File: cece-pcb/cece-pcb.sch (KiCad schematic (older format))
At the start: 26 parts, among them J1 SERIAL, J2 HTU21D, J3 Li-Ion Battery, J4 VAC, K1 SANYOU_SRD_Form_C, Q2 Q_NPN, U2 MCP73811T-420I-OT, U3 TLV75533PDBV

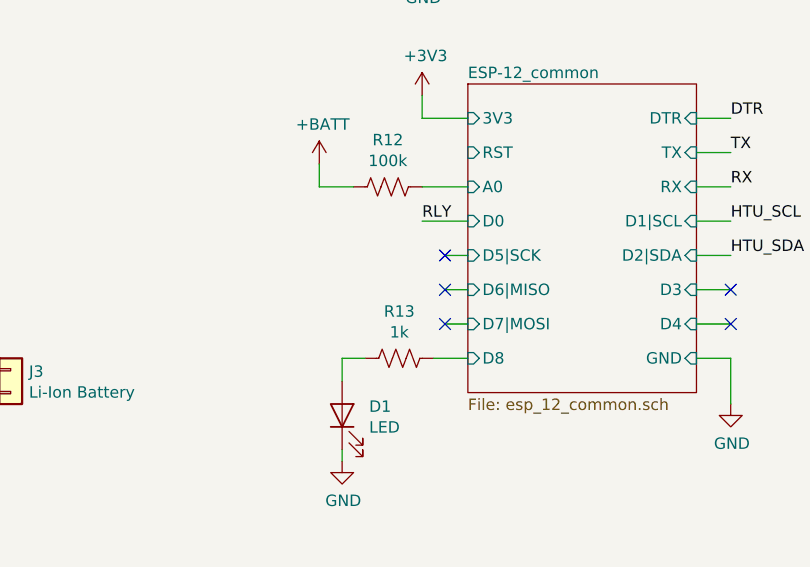
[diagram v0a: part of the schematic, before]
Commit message: Complete ESP-12 part of the PCB
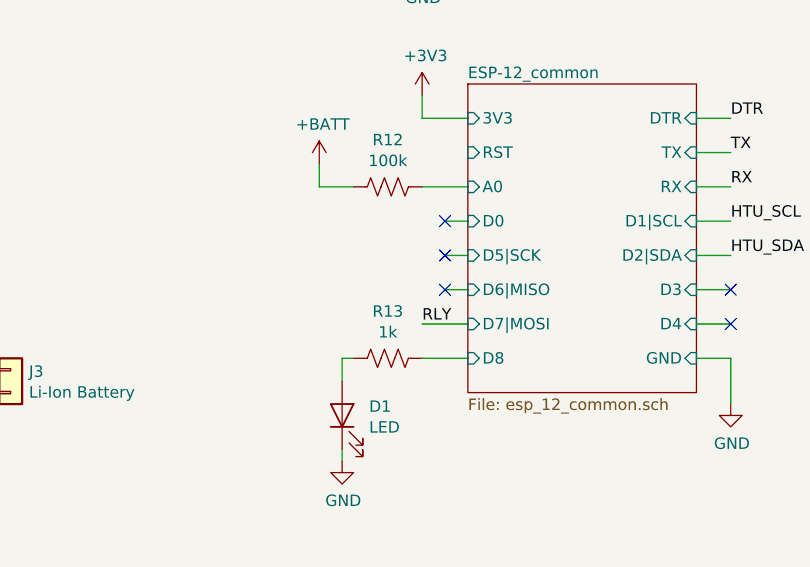
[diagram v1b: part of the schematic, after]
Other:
- moved on the sheet: R13
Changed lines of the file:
@@
 $EndSheet
 Wire Wire Line
-	5300 4150 5100 4150
+	5300 4600 5100 4600
 Wire Wire Line
 	6300 4150 6450 4150
 Wire Wire Line
 	6300 4300 6450 4300
-Text Label 5100 4150 0    50   ~ 0
+Text Label 5100 4600 0    50   ~ 0
 RLY
 Text Label 6450 4150 0    50   ~ 0
@@
 L Device:R_US R13
 U 1 1 5FE041BA
-P 5000 4750
-F 0 "R13" V 4795 4750 50  0000 C CNN
-F 1 "1k" V 4886 4750 50  0000 C CNN
-F 2 "Resistor_THT:R_Axial_DIN0207_L6.3mm_D2.5mm_P7.62mm_Horizontal" V 5040 4740 50  0001 C CNN
-F 3 "~" H 5000 4750 50  0001 C CNN
-	1    5000 4750
+P 4950 4750
+F 0 "R13" V 4745 4750 50  0000 C CNN
+F 1 "1k" V 4836 4750 50  0000 C CNN
+F 2 "Resistor_THT:R_Axial_DIN0207_L6.3mm_D2.5mm_P7.62mm_Horizontal" V 4990 4740 50  0001 C CNN
+F 3 "~" H 4950 4750 50  0001 C CNN
+	1    4950 4750
 	0    1    1    0
 $EndComp
@@
 $EndComp
 Wire Wire Line
-	5300 4750 5150 4750
-Wire Wire Line
-	4850 4750 4750 4750
+	5300 4750 5100 4750
+Wire Wire Line
+	4800 4750 4750 4750
 Wire Wire Line
 	4750 4750 4750 4850
@@
 NoConn ~ 5200 4300
 NoConn ~ 5200 4450
-NoConn ~ 5200 4600
+NoConn ~ 5200 4150
 NoConn ~ 6450 4600
 NoConn ~ 6450 4450
@@
 	5200 4450 5300 4450
 Wire Wire Line
-	5200 4600 5300 4600
+	5200 4150 5300 4150
 Wire Wire Line
 	6450 4600 6300 4600

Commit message: Finish first board revision
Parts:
- removed JP12: RLY_VCC, Jumper:SolderJumper-3_P1.3mm_Bridged12_Pad1.0x1.5mm, symbol Jumper:SolderJumper_3_Bridged12
- removed R12: 100k, Resistor_THT:R_Axial_DIN0207_L6.3mm_D2.5mm_P7.62mm_Horizontal, symbol Device:R_US
- added JP2: VBATT_A0, Jumper:SolderJumper-2_P1.3mm_Bridged_Pad1.0x1.5mm, symbol Jumper:SolderJumper_2_Bridged
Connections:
- wire segments 100 -> 90
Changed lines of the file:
@@
-	1    0    0    -1
-$EndComp
-$Comp
-L power:+3V3 #PWR018
-U 1 1 5FD89DF7
-P 7800 3050
-F 0 "#PWR018" H 7800 2900 50  0001 C CNN
-F 1 "+3V3" H 7815 3223 50  0000 C CNN
-F 2 "" H 7800 3050 50  0001 C CNN
-F 3 "" H 7800 3050 50  0001 C CNN
-	1    7800 3050
-	1    0    0    -1
-$EndComp
-$Comp
-L power:+5V #PWR019
-U 1 1 5FD8A15A
-P 8250 3050
-F 0 "#PWR019" H 8250 2900 50  0001 C CNN
-F 1 "+5V" H 8265 3223 50  0000 C CNN
-F 2 "" H 8250 3050 50  0001 C CNN
-F 3 "" H 8250 3050 50  0001 C CNN
-	1    8250 3050
 	1    0    0    -1
 $EndComp
@@
 	10200 2800 10050 2800
 Wire Wire Line
-	10050 2800 10050 2500
-Wire Wire Line
-	10050 2500 9150 2500
-Wire Wire Line
-	9150 2500 9150 2800
-Wire Wire Line
 	9150 2800 9300 2800
-Wire Wire Line
-	9000 3000 9000 2400
-Wire Wire Line
-	9000 2400 10150 2400
-Wire Wire Line
-	10150 2400 10150 2700
-Wire Wire Line
-	10150 2700 10200 2700
 $Comp
 L Converter_ACDC:HLK-PM01 PS1
@@
 Text Label 10050 3000 0    50   ~ 0
 LN
+Text Label 10050 2700 0    50   ~ 0
+NO
 Text Label 10050 2800 0    50   ~ 0
-NO
-Text Label 10050 2400 0    50   ~ 0
 NC
 Wire Wire Line
@@
 	8550 3800 8550 3750
 Wire Wire Line
-	9000 3000 9300 3000
+	9150 3000 9300 3000
 $Comp
 L Battery_Management:MCP73811T-420I-OT U2
@@
 Wire Wire Line
 	2550 5100 2550 5200
-$Comp
-L Device:R_US R12
-U 1 1 5FDFCF50
-P 4950 4000
-F 0 "R12" V 4745 4000 50  0000 C CNN
-F 1 "100k" V 4836 4000 50  0000 C CNN
-F 2 "Resistor_THT:R_Axial_DIN0207_L6.3mm_D2.5mm_P7.62mm_Horizontal" V 4990 3990 50  0001 C CNN
-F 3 "~" H 4950 4000 50  0001 C CNN
-	1    4950 4000
-	0    1    1    0
-$EndComp
 Wire Wire Line
 	5100 4000 5300 4000
-$Comp
-L power:+BATT #PWR023
-U 1 1 5FDFFC00
-P 4650 3900
-F 0 "#PWR023" H 4650 3750 50  0001 C CNN
-F 1 "+BATT" H 4665 4073 50  0000 C CNN
-F 2 "" H 4650 3900 50  0001 C CNN
-F 3 "" H 4650 3900 50  0001 C CNN
-	1    4650 3900
-	1    0    0    -1
-$EndComp
-Wire Wire Line
-	4650 3900 4650 4000
 Wire Wire Line
 	4650 4000 4800 4000
@@
 Wire Wire Line
 	8250 5650 8000 5650
-$Comp
-L Jumper:SolderJumper_3_Bridged12 JP12
-U 1 1 5FD8AB22
-P 8250 3300
-F 0 "JP12" V 8204 3368 50  0000 L CNN
-F 1 "RLY_VCC" V 8295 3368 50  0000 L CNN
-F 2 "Jumper:SolderJumper-3_P1.3mm_Bridged12_Pad1.0x1.5mm" H 8250 3300 50  0001 C CNN
-F 3 "~" H 8250 3300 50  0001 C CNN
-	1    8250 3300
-	0    -1   1    0
-$EndComp
-Wire Wire Line
-	8550 3300 8400 3300
-Connection ~ 8550 3300
-Wire Wire Line
-	8250 3050 8250 3100
-Wire Wire Line
-	7800 3050 7800 3500
-Wire Wire Line
-	7800 3500 8250 3500
+Wire Wire Line
+	10050 2700 10200 2700
+Text Label 9150 2800 0    50   ~ 0
+NO
+Text Label 9150 3000 0    50   ~ 0
+NC
+$Comp
+L Jumper:SolderJumper_2_Bridged JP2
+U 1 1 5FCD2589
+P 4950 4000
+F 0 "JP2" H 4950 4205 50  0000 C CNN
+F 1 "VBATT_A0" H 4950 4114 50  0000 C CNN
+F 2 "Jumper:SolderJumper-2_P1.3mm_Bridged_Pad1.0x1.5mm" H 4950 4000 50  0001 C CNN
+F 3 "~" H 4950 4000 50  0001 C CNN
+	1    4950 4000
+	1    0    0    -1
+$EndComp
+Wire Wire Line
+	4650 3900 4650 4000
+$Comp
+L power:+BATT #PWR023
+U 1 1 5FDFFC00
+P 4650 3900
+F 0 "#PWR023" H 4650 3750 50  0001 C CNN
+F 1 "+BATT" H 4665 4073 50  0000 C CNN
+F 2 "" H 4650 3900 50  0001 C CNN
+F 3 "" H 4650 3900 50  0001 C CNN
+	1    4650 3900
+	1    0    0    -1
+$EndComp
+$Comp
+L power:+BATT #PWR?
+U 1 1 5FD3EF92
+P 9200 3300
+F 0 "#PWR?" H 9200 3150 50  0001 C CNN
+F 1 "+BATT" H 9215 3473 50  0000 C CNN
+F 2 "" H 9200 3300 50  0001 C CNN
+F 3 "" H 9200 3300 50  0001 C CNN
+	1    9200 3300
+	1    0    0    -1
+$EndComp
 $EndSCHEMATC

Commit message: More touches to the layout. Almost finished
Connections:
- net +3V3: now also J1.1 (Pin_1); no longer J1.5 (Pin_5)
- net GND: now also J1.5 (Pin_5); no longer J1.1 (Pin_1)
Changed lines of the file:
@@
 $EndComp
-Wire Wire Line
-	5100 2600 5250 2600
 Wire Wire Line
 	5100 2700 5250 2700
@@
 Wire Wire Line
 	5250 2900 5100 2900
-Wire Wire Line
-	5100 3000 5250 3000
 $Comp
 L power:+3V3 #PWR0103
 U 1 1 5FD72E0B
-P 5100 2600
-F 0 "#PWR0103" H 5100 2450 50  0001 C CNN
-F 1 "+3V3" H 5115 2773 50  0000 C CNN
-F 2 "" H 5100 2600 50  0001 C CNN
-F 3 "" H 5100 2600 50  0001 C CNN
-	1    5100 2600
+P 4700 3000
+F 0 "#PWR0103" H 4700 2850 50  0001 C CNN
+F 1 "+3V3" H 4715 3173 50  0000 C CNN
+F 2 "" H 4700 3000 50  0001 C CNN
+F 3 "" H 4700 3000 50  0001 C CNN
+	1    4700 3000
 	1    0    0    -1
 $EndComp
@@
 L power:GND #PWR0104
 U 1 1 5FD73334
-P 5100 3000
-F 0 "#PWR0104" H 5100 2750 50  0001 C CNN
-F 1 "GND" H 5105 2827 50  0000 C CNN
-F 2 "" H 5100 3000 50  0001 C CNN
-F 3 "" H 5100 3000 50  0001 C CNN
-	1    5100 3000
+P 4950 2600
+F 0 "#PWR0104" H 4950 2350 50  0001 C CNN
+F 1 "GND" H 4955 2427 50  0000 C CNN
+F 2 "" H 4950 2600 50  0001 C CNN
+F 3 "" H 4950 2600 50  0001 C CNN
+	1    4950 2600
 	1    0    0    -1
 $EndComp
@@
 $EndComp
 $Comp
-L power:+BATT #PWR?
+L power:+BATT #PWR0109
 U 1 1 5FD3EF92
 P 9200 3300
-F 0 "#PWR?" H 9200 3150 50  0001 C CNN
+F 0 "#PWR0109" H 9200 3150 50  0001 C CNN
 F 1 "+BATT" H 9215 3473 50  0000 C CNN
 F 2 "" H 9200 3300 50  0001 C CNN
@@
 	1    0    0    -1
 $EndComp
+Wire Wire Line
+	4950 2600 5250 2600
+Wire Wire Line
+	4700 3000 5250 3000
 $EndSCHEMATC

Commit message: Add jumper to send 5V directly to the LDO if no battery is installed
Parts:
- added JP3: VBATT 5V, Jumper:SolderJumper-2_P1.3mm_Open_Pad1.0x1.5mm, symbol Jumper:SolderJumper_2_Open
- J4: footprint TerminalBlock:TerminalBlock_bornier-4_P5.08mm -> TerminalBlock:TerminalBlock_bornier-5_P5.08mm; symbol Connector:Screw_Terminal_01x04 -> Connector:Screw_Terminal_01x05
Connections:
- net +5V: now also JP3.1 (A)
- net +BATT: now also JP3.2 (B)
- net C: now also J4.2 (Pin_2); no longer J4.3 (Pin_3), PS1.2 (AC/N)
- net NC: now also J4.3 (Pin_3); no longer J4.2 (Pin_2)
- net LN renamed ACL
- net ACL: now also J4.5 (Pin_5); no longer J4.4 (Pin_4)
- new net ACN: J4.4 (Pin_4), PS1.2 (AC/N)
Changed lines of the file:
@@
 RLY
 $Comp
-L Connector:Screw_Terminal_01x04 J4
+L Connector:Screw_Terminal_01x05 J4
 U 1 1 5FD96487
-P 10400 2800
-F 0 "J4" H 10480 2792 50  0000 L CNN
-F 1 "VAC" H 10480 2701 50  0000 L CNN
-F 2 "TerminalBlock:TerminalBlock_bornier-4_P5.08mm" H 10400 2800 50  0001 C CNN
-F 3 "~" H 10400 2800 50  0001 C CNN
-	1    10400 2800
-	1    0    0    -1
-$EndComp
-Wire Wire Line
-	10200 2900 9900 2900
-Wire Wire Line
-	10200 2800 10050 2800
+P 10450 2250
+F 0 "J4" H 10530 2242 50  0000 L CNN
+F 1 "VAC" H 10530 2151 50  0000 L CNN
+F 2 "TerminalBlock:TerminalBlock_bornier-5_P5.08mm" H 10450 2250 50  0001 C CNN
+F 3 "~" H 10450 2250 50  0001 C CNN
+	1    10450 2250
+	1    0    0    -1
+$EndComp
+Wire Wire Line
+	10250 2250 10100 2250
 Wire Wire Line
 	9150 2800 9300 2800
@@
 $EndComp
 Wire Wire Line
-	10200 3000 10050 3000
-Text Label 10050 2900 0    50   ~ 0
+	10250 2450 10100 2450
+Text Label 10000 2900 0    50   ~ 0
 C
-Text Label 10050 3000 0    50   ~ 0
-LN
-Text Label 10050 2700 0    50   ~ 0
+Text Label 10100 2050 0    50   ~ 0
 NO
-Text Label 10050 2800 0    50   ~ 0
+Text Label 10100 2250 0    50   ~ 0
 NC
 Wire Wire Line
-	1400 2750 1300 2750
-Wire Wire Line
-	1400 2950 1300 2950
-Text Label 1300 2750 0    50   ~ 0
-LN
-Text Label 1300 2950 0    50   ~ 0
-C
+	1400 2750 1250 2750
 $Comp
 L power:GND #PWR015
@@
 P 2000 4700
 F 0 "U2" H 2150 4600 50  0000 L CNN
-F 1 "MCP73811T-420I-OT" H 2050 4950 50  0000 L CNN
+F 1 "MCP73811T-420I-OT" H 1700 4400 50  0000 L CNN
 F 2 "Package_TO_SOT_SMD:SOT-23-5" H 2050 4450 50  0001 L CNN
 F 3 "http://ww1.microchip.com/downloads/en/DeviceDoc/22036b.pdf" H 1750 4950 50  0001 C CNN
@@
 	8250 5650 8000 5650
 Wire Wire Line
-	10050 2700 10200 2700
+	10100 2150 10250 2150
 Text Label 9150 2800 0    50   ~ 0
 NO
@@
 Wire Wire Line
 	4700 3000 5250 3000
+Wire Wire Line
+	9900 2900 10000 2900
+Wire Wire Line
+	10100 2350 10250 2350
+Wire Wire Line
+	10100 2050 10250 2050
+Text Label 10100 2150 0    50   ~ 0
+C
+Text Label 1250 2750 0    50   ~ 0
+ACL
+Text Label 1250 2950 0    50   ~ 0
+ACN
+Wire Wire Line
+	1250 2950 1400 2950
+Text Label 10100 2450 0    50   ~ 0
+ACL
+Text Label 10100 2350 0    50   ~ 0
+ACN
+$Comp
+L Jumper:SolderJumper_2_Open JP3
+U 1 1 5FD1A80F
+P 2300 4350
+F 0 "JP3" H 2300 4555 50  0000 C CNN
+F 1 "VBATT 5V" H 2300 4464 50  0000 C CNN
+F 2 "Jumper:SolderJumper-2_P1.3mm_Open_Pad1.0x1.5mm" H 2300 4350 50  0001 C CNN
+F 3 "~" H 2300 4350 50  0001 C CNN
+	1    2300 4350
+	1    0    0    -1
+$EndComp
+Wire Wire Line
+	2150 4350 2000 4350
+Wire Wire Line
+	2550 4350 2550 4600
+Wire Wire Line
+	2550 4350 2450 4350
 $EndSCHEMATC

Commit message: Fix wrong footprint for the pin headers
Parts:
- J1: footprint Connector_PinHeader_1.27mm:PinHeader_1x05_P1.27mm_Vertical -> Connector_PinHeader_2.54mm:PinHeader_1x05_P2.54mm_Vertical
- J2: footprint Connector_PinHeader_1.27mm:PinHeader_1x04_P1.27mm_Vertical -> Connector_PinHeader_2.54mm:PinHeader_1x04_P2.54mm_Vertical
- J3: footprint Connector_PinHeader_1.27mm:PinHeader_1x02_P1.27mm_Vertical -> Connector_PinHeader_2.54mm:PinHeader_1x02_P2.54mm_Vertical
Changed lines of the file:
@@
 F 0 "J1" H 5422 2732 50  0000 R CNN
 F 1 "SERIAL" H 5422 2823 50  0000 R CNN
-F 2 "Connector_PinHeader_1.27mm:PinHeader_1x05_P1.27mm_Vertical" H 5450 2800 50  0001 C CNN
+F 2 "Connector_PinHeader_2.54mm:PinHeader_1x05_P2.54mm_Vertical" H 5450 2800 50  0001 C CNN
 F 3 "~" H 5450 2800 50  0001 C CNN
 	1    5450 2800
@@
 F 0 "J2" H 6628 2726 50  0000 L CNN
 F 1 "HTU21D" H 6628 2635 50  0000 L CNN
-F 2 "Connector_PinHeader_1.27mm:PinHeader_1x04_P1.27mm_Vertical" H 6600 2750 50  0001 C CNN
+F 2 "Connector_PinHeader_2.54mm:PinHeader_1x04_P2.54mm_Vertical" H 6600 2750 50  0001 C CNN
 F 3 "~" H 6600 2750 50  0001 C CNN
 	1    6600 2750
@@
 F 0 "J3" H 3380 4792 50  0000 L CNN
 F 1 "Li-Ion Battery" H 3380 4701 50  0000 L CNN
-F 2 "Connector_PinHeader_1.27mm:PinHeader_1x02_P1.27mm_Vertical" H 3300 4800 50  0001 C CNN
+F 2 "Connector_PinHeader_2.54mm:PinHeader_1x02_P2.54mm_Vertical" H 3300 4800 50  0001 C CNN
 F 3 "~" H 3300 4800 50  0001 C CNN
 	1    3300 4800

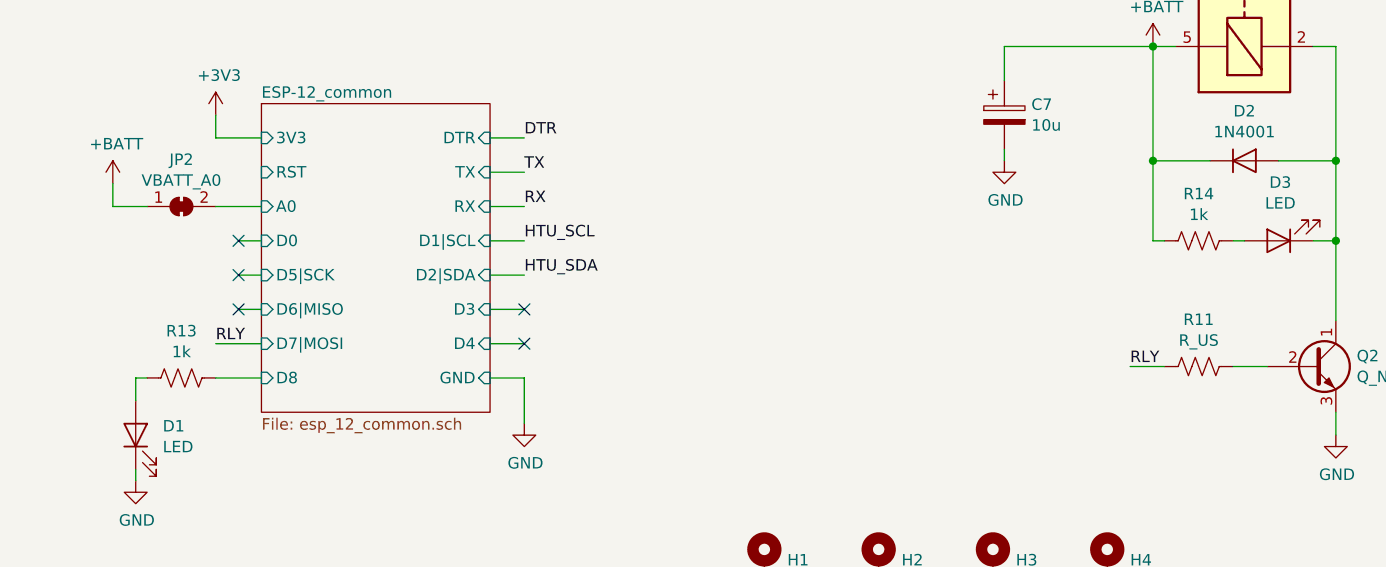
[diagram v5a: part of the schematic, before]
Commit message: Update component values
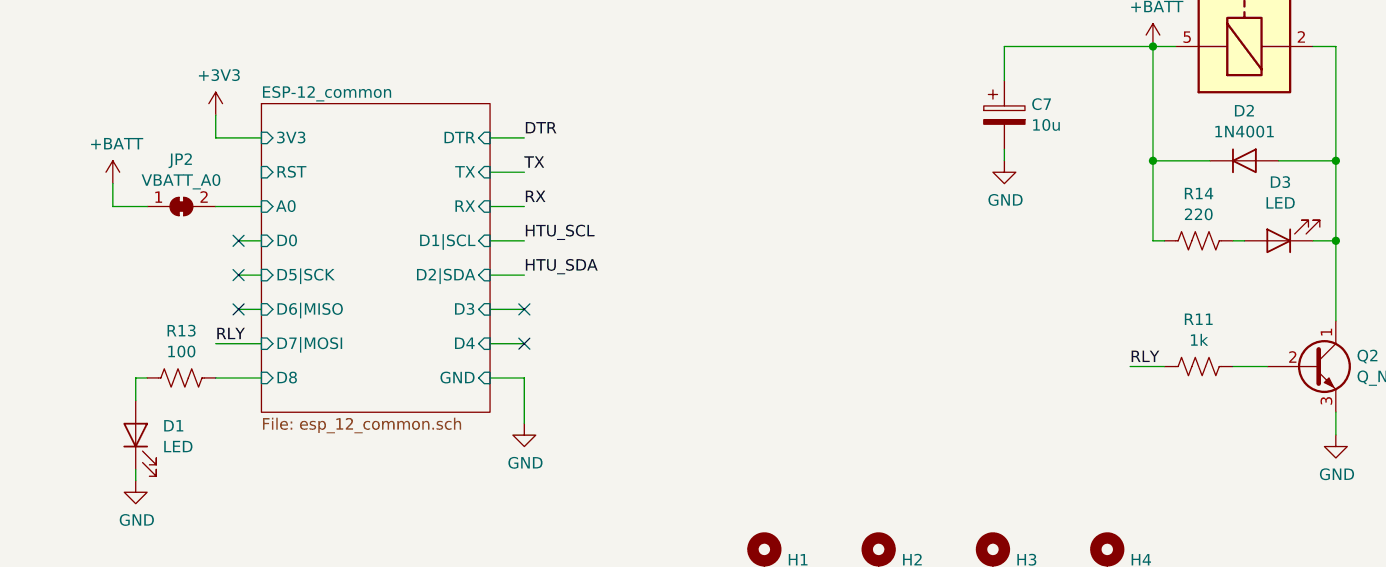
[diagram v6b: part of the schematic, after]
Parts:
- R11: value R_US -> 1k
- R13: value 1k -> 100
- R14: value 1k -> 220
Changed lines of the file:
@@
 P 9400 4700
 F 0 "R11" V 9195 4700 50  0000 C CNN
-F 1 "R_US" V 9286 4700 50  0000 C CNN
+F 1 "1k" V 9286 4700 50  0000 C CNN
 F 2 "Resistor_THT:R_Axial_DIN0207_L6.3mm_D2.5mm_P7.62mm_Horizontal" V 9440 4690 50  0001 C CNN
 F 3 "~" H 9400 4700 50  0001 C CNN
@@
 P 4950 4750
 F 0 "R13" V 4745 4750 50  0000 C CNN
-F 1 "1k" V 4836 4750 50  0000 C CNN
+F 1 "100" V 4836 4750 50  0000 C CNN
 F 2 "Resistor_THT:R_Axial_DIN0207_L6.3mm_D2.5mm_P7.62mm_Horizontal" V 4990 4740 50  0001 C CNN
 F 3 "~" H 4950 4750 50  0001 C CNN
@@
 P 9400 4150
 F 0 "R14" V 9195 4150 50  0000 C CNN
-F 1 "1k" V 9286 4150 50  0000 C CNN
+F 1 "220" V 9286 4150 50  0000 C CNN
 F 2 "Resistor_THT:R_Axial_DIN0207_L6.3mm_D2.5mm_P7.62mm_Horizontal" V 9440 4140 50  0001 C CNN
 F 3 "~" H 9400 4150 50  0001 C CNN

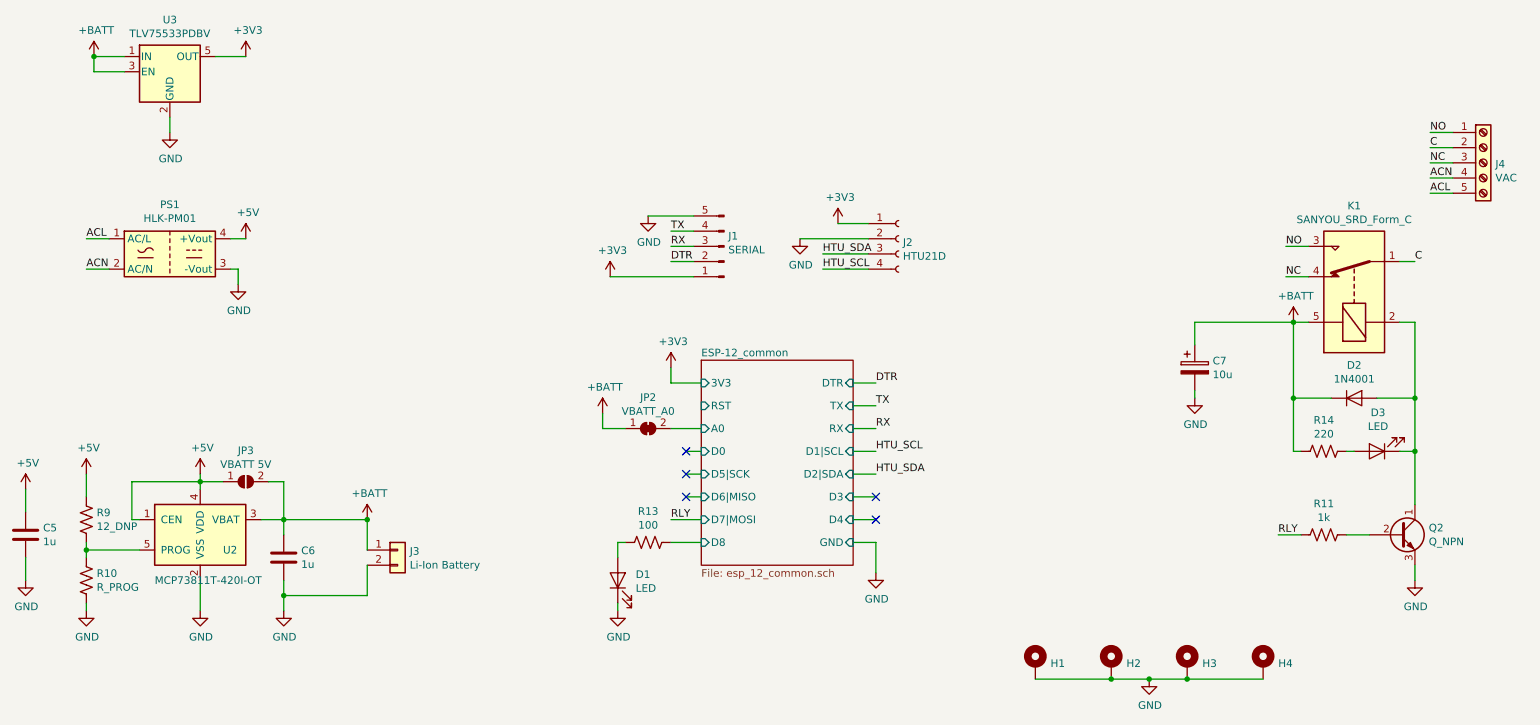
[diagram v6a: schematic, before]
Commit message: Update schematic references to reflect hierarchy
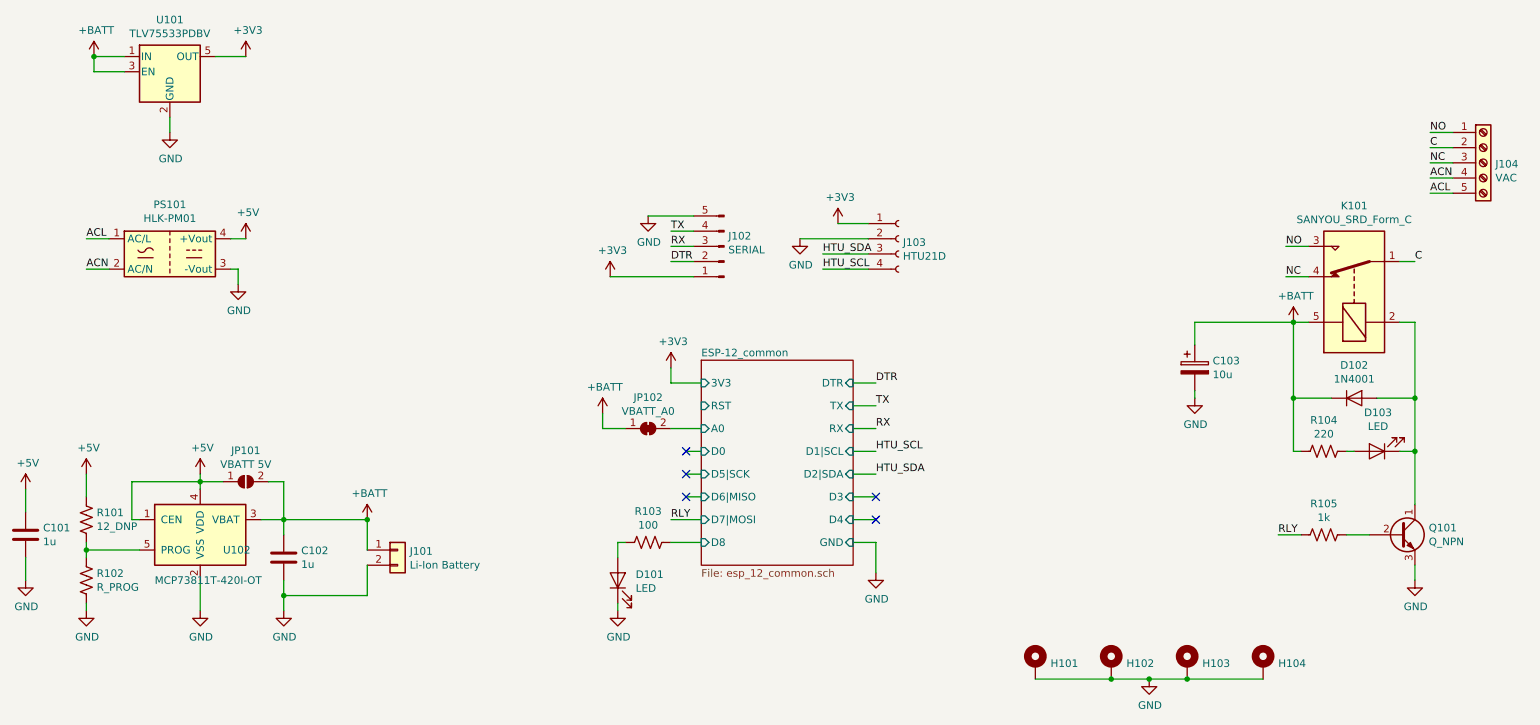
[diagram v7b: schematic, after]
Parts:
- renumbered C5 to C101, C6 to C102, C7 to C103, D1 to D101, D2 to D102, D3 to D103, H1 to H101, H2 to H102, H3 to H103, H4 to H104, J3 to J101, J1 to J102, J2 to J103, J4 to J104, JP3 to JP101, JP2 to JP102, K1 to K101, PS1 to PS101, Q2 to Q101, R9 to R101, R10 to R102, R13 to R103, R14 to R104, R11 to R105, U3 to U101, U2 to U102
